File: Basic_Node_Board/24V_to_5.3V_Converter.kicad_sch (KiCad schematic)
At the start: 13 parts, among them J2 Conn_01x02, U1 TPS54560BQDDARQ1

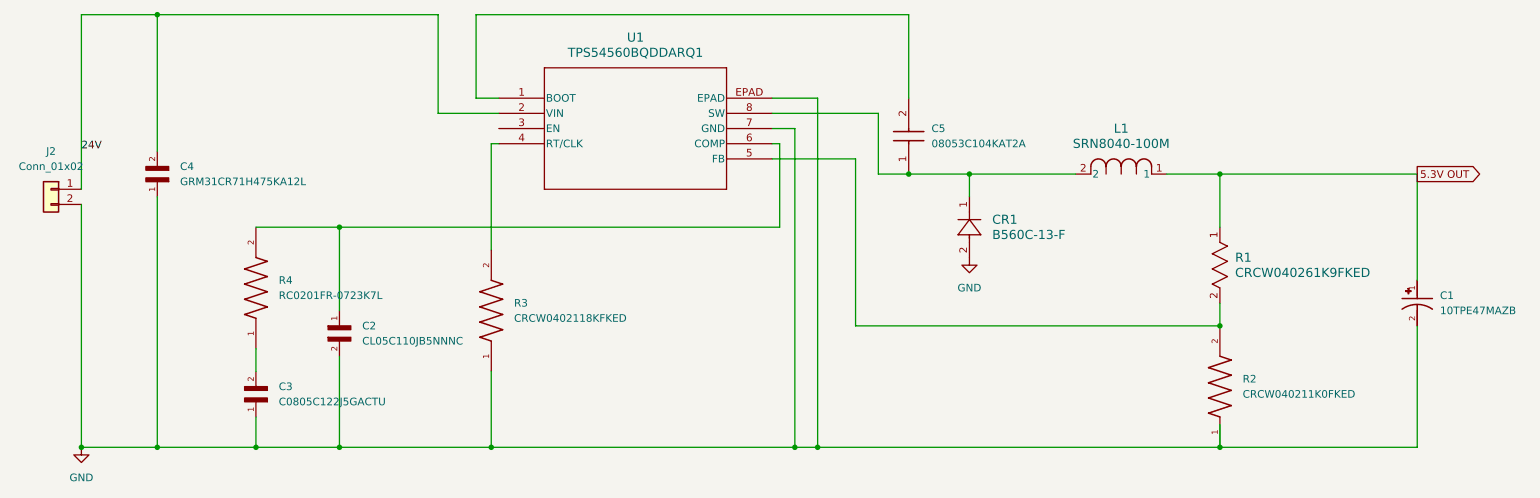
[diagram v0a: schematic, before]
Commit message: Power Distribution PCB KiCAD Schematic
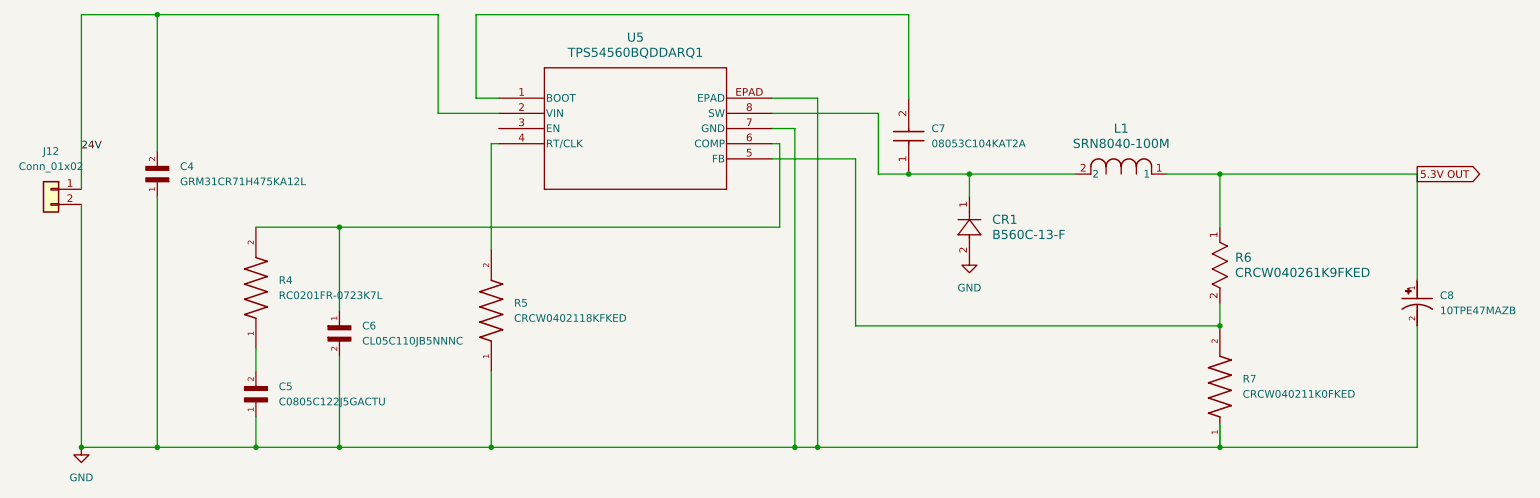
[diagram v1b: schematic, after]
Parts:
- renumbered C3 to C5, C2 to C6, C5 to C7, C1 to C8, J2 to J12, R3 to R5, R1 to R6, R2 to R7, U1 to U5
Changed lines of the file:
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@@
 		(dnp no)
 		(fields_autoplaced yes)
-		(property "Reference" "R3"
+		(property "Reference" "R5"
 			(at 107.95 105.4099 90)
 			(effects
@@
 			(project "Basic_Node_Board"
 				(path "/9602f2a9-59de-4c89-af09-0033871e87a5/10d14dc3-2b83-46d1-82b9-6acb009ce1b4"
-					(reference "R6")
+					(reference "R5")
 					(unit 1)
 				)
@@
 		(on_board yes)
 		(dnp no)
-		(property "Reference" "C3"
+		(property "Reference" "C5"
 			(at 68.58 119.3799 90)
 			(effects
@@
 		(dnp no)
 		(fields_autoplaced yes)
-		(property "Reference" "U1"
+		(property "Reference" "U5"
 			(at 128.27 60.96 0)
 			(effects
@@
 			(project "Basic_Node_Board"
 				(path "/9602f2a9-59de-4c89-af09-0033871e87a5/10d14dc3-2b83-46d1-82b9-6acb009ce1b4"
-					(reference "U6")
+					(reference "U5")
 					(unit 1)
 				)
@@
 		(dnp no)
 		(fields_autoplaced yes)
-		(property "Reference" "C2"
+		(property "Reference" "C6"
 			(at 82.55 109.2199 90)
 			(effects
@@
 			(project "Basic_Node_Board"
 				(path "/9602f2a9-59de-4c89-af09-0033871e87a5/10d14dc3-2b83-46d1-82b9-6acb009ce1b4"
-					(reference "R5")
+					(reference "R4")
 					(unit 1)
 				)
@@
 		(dnp no)
 		(fields_autoplaced yes)
-		(property "Reference" "#PWR03"
+		(property "Reference" "#PWR09"
 			(at 184.15 104.14 0)
 			(effects
@@
 			(project "Basic_Node_Board"
 				(path "/9602f2a9-59de-4c89-af09-0033871e87a5/10d14dc3-2b83-46d1-82b9-6acb009ce1b4"
-					(reference "#PWR0101")
+					(reference "#PWR09")
 					(unit 1)
 				)
@@
 		(dnp no)
 		(fields_autoplaced yes)
-		(property "Reference" "R1"
+		(property "Reference" "R6"
 			(at 228.6 97.7899 90)
 			(effects
@@
 			(project "Basic_Node_Board"
 				(path "/9602f2a9-59de-4c89-af09-0033871e87a5/10d14dc3-2b83-46d1-82b9-6acb009ce1b4"
-					(reference "R7")
+					(reference "R6")
 					(unit 1)
 				)
@@
 		(dnp no)
 		(fields_autoplaced yes)
-		(property "Reference" "#PWR02"
+		(property "Reference" "#PWR08"
 			(at 35.56 135.89 0)
 			(effects
@@
 			(project "Basic_Node_Board"
 				(path "/9602f2a9-59de-4c89-af09-0033871e87a5/10d14dc3-2b83-46d1-82b9-6acb009ce1b4"
-					(reference "#PWR0102")
+					(reference "#PWR08")
 					(unit 1)
 				)
@@
 		(dnp no)
 		(fields_autoplaced yes)
-		(property "Reference" "C1"
+		(property "Reference" "C8"
 			(at 262.89 104.1399 90)
 			(effects
@@
 			(project "Basic_Node_Board"
 				(path "/9602f2a9-59de-4c89-af09-0033871e87a5/10d14dc3-2b83-46d1-82b9-6acb009ce1b4"
-					(reference "C7")
+					(reference "C8")
 					(unit 1)
 				)
@@
 		(dnp no)
 		(fields_autoplaced yes)
-		(property "Reference" "C5"
+		(property "Reference" "C7"
 			(at 177.8 76.1999 90)
 			(effects
@@
 			(project ""
 				(path "/9602f2a9-59de-4c89-af09-0033871e87a5/10d14dc3-2b83-46d1-82b9-6acb009ce1b4"
-					(reference "C8")
+					(reference "C7")
 					(unit 1)
 				)
@@
 		(dnp no)
 		(fields_autoplaced yes)
-		(property "Reference" "R2"
+		(property "Reference" "R7"
 			(at 229.87 118.1099 90)
 			(effects
@@
 			(project "Basic_Node_Board"
 				(path "/9602f2a9-59de-4c89-af09-0033871e87a5/10d14dc3-2b83-46d1-82b9-6acb009ce1b4"
-					(reference "R8")
+					(reference "R7")
 					(unit 1)
 				)
@@
 		(dnp no)
 		(fields_autoplaced yes)
-		(property "Reference" "J2"
+		(property "Reference" "J12"
 			(at 30.48 80.01 0)
 			(effects
@@
 			(project "Basic_Node_Board"
 				(path "/9602f2a9-59de-4c89-af09-0033871e87a5/10d14dc3-2b83-46d1-82b9-6acb009ce1b4"
-					(reference "J2")
-					(unit 1)
-				)
+					(reference "J12")
+					(unit 1)
+				)

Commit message: made changes to buck converter - jacob Kyeyune
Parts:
- C1: renamed from C8; value 10TPE47MAZB -> 47uF
- C2: renamed from C6; value CL05C110JB5NNNC -> 10pF
- C3: renamed from C5; value C0805C122J5GACTU -> 12nF
- C4: value GRM31CR71H475KA12L -> 4.7uF
- C5: renamed from C7; value 08053C104KAT2A -> 100nF
- CR1: value B560C-13-F -> SS34
- L1: value SRN8040-100M -> 27uH
- R1: renamed from R6; value CRCW040261K9FKED -> 61.1kOhm
- R2: renamed from R7; value CRCW040211K0FKED -> 11kOhns
- R3: renamed from R5; value CRCW0402118KFKED -> 147kOhms
- R4: value RC0201FR-0723K7L -> 15.4kOhms
- renumbered J12 to J2, U5 to U1
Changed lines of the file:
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@@
 		(dnp no)
 		(fields_autoplaced yes)
-		(property "Reference" "R5"
+		(property "Reference" "R3"
 			(at 107.95 105.4099 90)
 			(effects
@@
 			)
 		)
-		(property "Value" "CRCW0402118KFKED"
+		(property "Value" "147kOhms"
 			(at 107.95 107.9499 90)
 			(effects
@@
 			)
 		)
-		(property "Value" "B560C-13-F"
+		(property "Value" "SS34"
 			(at 187.96 93.9799 90)
 			(effects
@@
 		(on_board yes)
 		(dnp no)
-		(property "Reference" "C5"
+		(property "Reference" "C3"
 			(at 68.58 119.3799 90)
 			(effects
@@
 			)
 		)
-		(property "Value" "C0805C122J5GACTU"
+		(property "Value" "12nF"
 			(at 68.58 121.9199 90)
 			(effects
@@
 		(dnp no)
 		(fields_autoplaced yes)
-		(property "Reference" "U5"
+		(property "Reference" "U1"
 			(at 128.27 60.96 0)
 			(effects
@@
 		(dnp no)
 		(fields_autoplaced yes)
-		(property "Reference" "C6"
+		(property "Reference" "C2"
 			(at 82.55 109.2199 90)
 			(effects
@@
 			)
 		)
-		(property "Value" "CL05C110JB5NNNC"
+		(property "Value" "10pF"
 			(at 82.55 111.7599 90)
 			(effects
@@
 			)
 		)
-		(property "Value" "RC0201FR-0723K7L"
+		(property "Value" "15.4kOhms"
 			(at 68.58 104.1399 90)
 			(effects
@@
 		(dnp no)
 		(fields_autoplaced yes)
-		(property "Reference" "#PWR09"
+		(property "Reference" "#PWR03"
 			(at 184.15 104.14 0)
 			(effects
@@
 			)
 		)
-		(property "Value" "GRM31CR71H475KA12L"
+		(property "Value" "4.7uF"
 			(at 52.07 85.0899 90)
 			(effects
@@
 		(dnp no)
 		(fields_autoplaced yes)
-		(property "Reference" "R6"
+		(property "Reference" "R1"
 			(at 228.6 97.7899 90)
 			(effects
@@
 			)
 		)
-		(property "Value" "CRCW040261K9FKED"
+		(property "Value" "61.1kOhm"
 			(at 228.6 100.3299 90)
 			(effects
@@
 			)
 		)
-		(property "Value" "SRN8040-100M"
+		(property "Value" "27uH"
 			(at 209.55 78.74 0)
 			(effects
@@
 		(dnp no)
 		(fields_autoplaced yes)
-		(property "Reference" "#PWR08"
+		(property "Reference" "#PWR02"
 			(at 35.56 135.89 0)
 			(effects
@@
 		(dnp no)
 		(fields_autoplaced yes)
-		(property "Reference" "C8"
+		(property "Reference" "C1"
 			(at 262.89 104.1399 90)
 			(effects
@@
 			)
 		)
-		(property "Value" "10TPE47MAZB"
+		(property "Value" "47uF"
 			(at 262.89 106.6799 90)
 			(effects
@@
 		(dnp no)
 		(fields_autoplaced yes)
-		(property "Reference" "C7"
+		(property "Reference" "C5"
 			(at 177.8 76.1999 90)
 			(effects
@@
 			)
 		)
-		(property "Value" "08053C104KAT2A"
+		(property "Value" "100nF"
 			(at 177.8 78.7399 90)
 			(effects
@@
 		(dnp no)
 		(fields_autoplaced yes)
-		(property "Reference" "R7"
+		(property "Reference" "R2"
 			(at 229.87 118.1099 90)
 			(effects
@@
 			)
 		)
-		(property "Value" "CRCW040211K0FKED"
+		(property "Value" "11kOhns"
 			(at 229.87 120.6499 90)
 			(effects
@@
 		(dnp no)
 		(fields_autoplaced yes)
-		(property "Reference" "J12"
+		(property "Reference" "J2"
 			(at 30.48 80.01 0)
 			(effects
